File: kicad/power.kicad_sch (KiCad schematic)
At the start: 27 parts, among them U2 RT9471GQW, U3 MCP1663T-E/MNY, U4 MCP1603-330I/MC

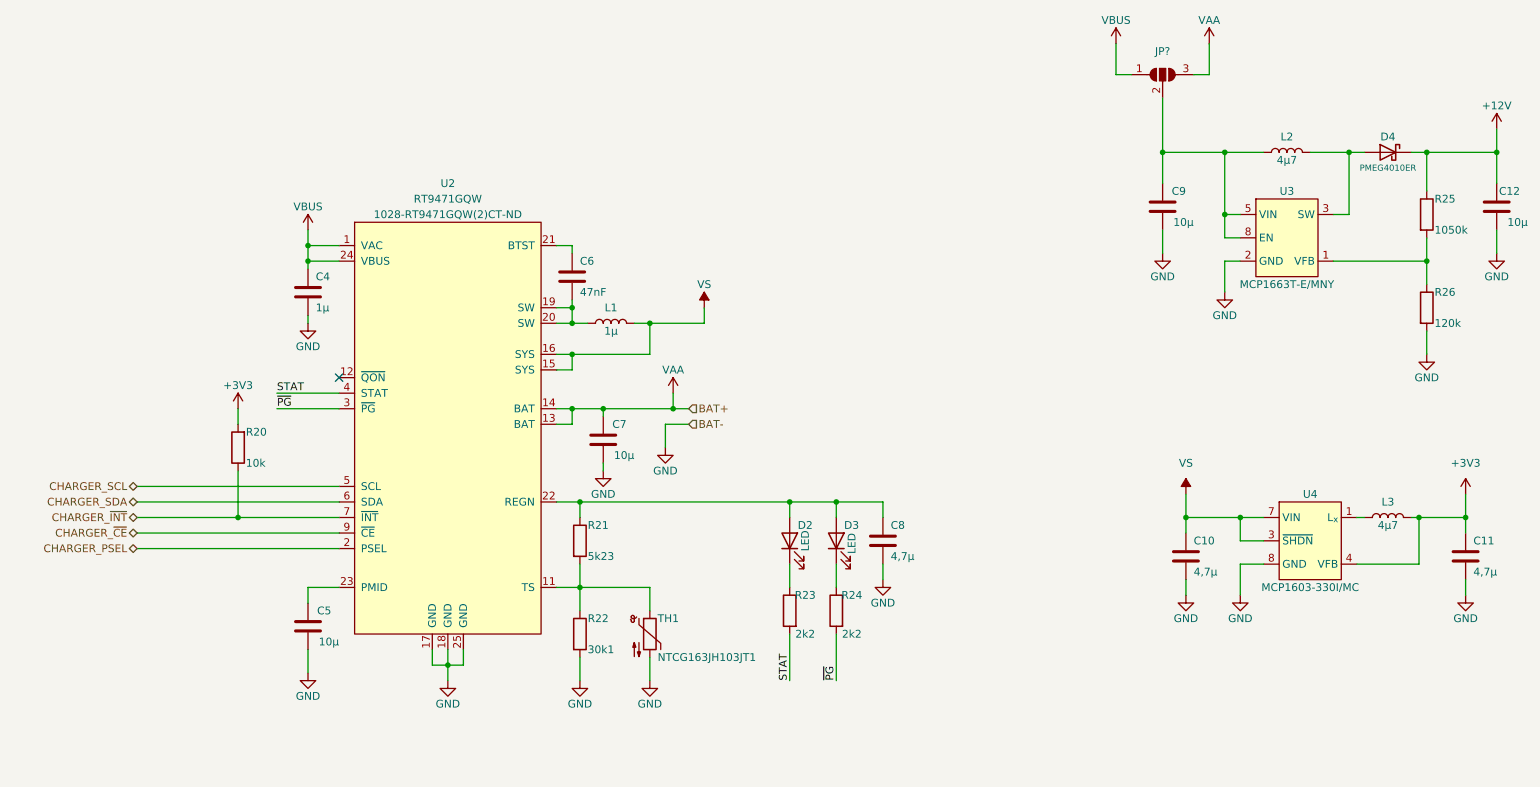
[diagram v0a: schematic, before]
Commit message: refactor KiCAD Project to v6
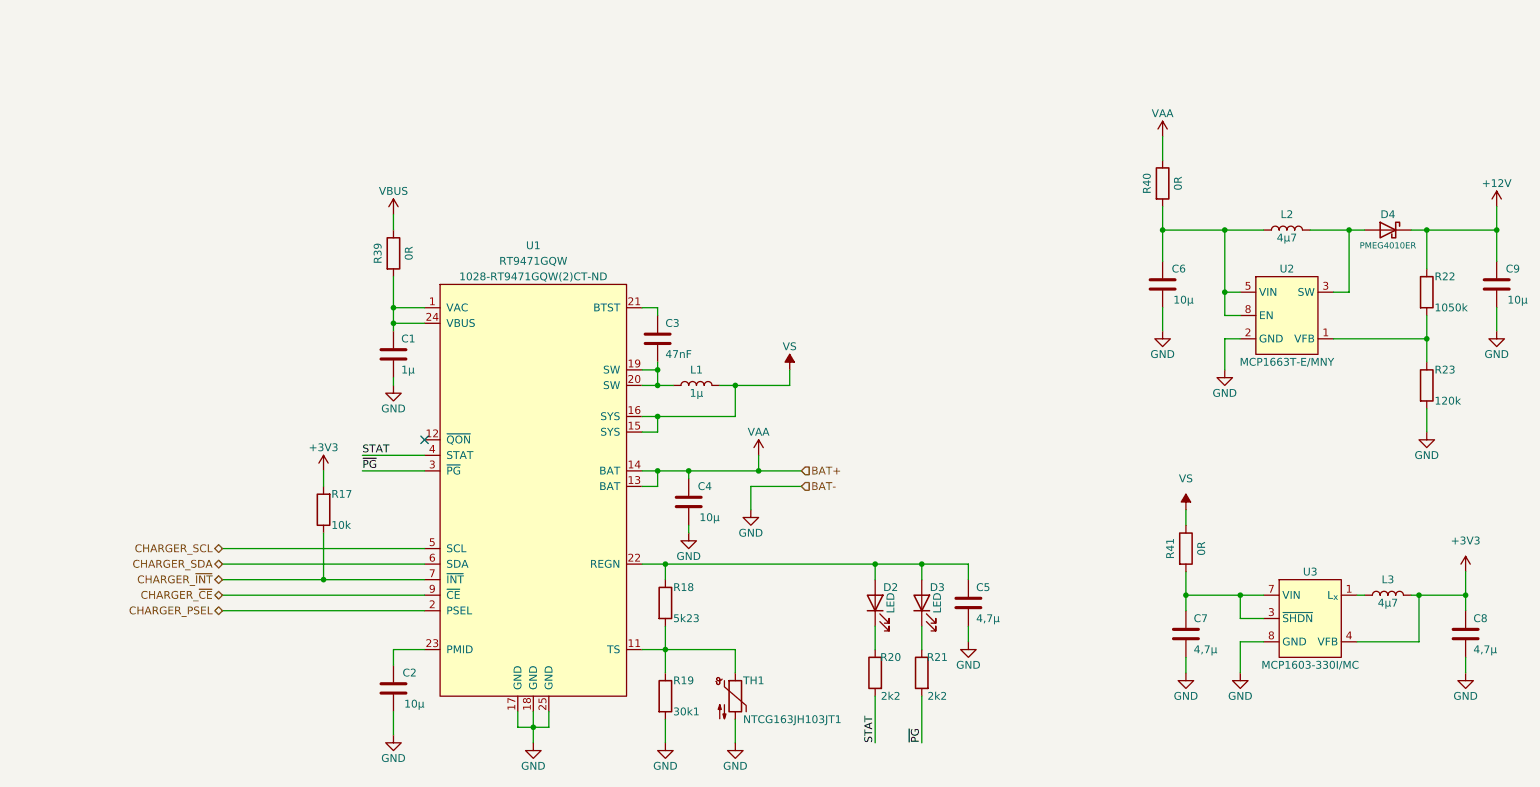
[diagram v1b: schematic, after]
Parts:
- removed C10, C11: 4,7µ, Capacitor_SMD:C_0603_1608Metric, symbol Device:C
- removed C12: 10µ, Capacitor_SMD:C_0603_1608Metric, symbol Device:C
- removed JP?: SolderJumper_3_Open, Jumper:SolderJumper-3_P1.3mm_Open_Pad1.0x1.5mm_NumberLabels, symbol Jumper:SolderJumper_3_Open
- removed R24: 2k2, Resistor_SMD:R_0603_1608Metric, symbol Device:R
- removed R25: 1050k, Resistor_SMD:R_0603_1608Metric, symbol Device:R
- removed R26: 120k, Resistor_SMD:R_0603_1608Metric, symbol Device:R
- removed U2: RT9471GQW, Package_DFN_QFN:WQFN-24-1EP_4x4mm_P0.5mm_EP2.6x2.6mm_ThermalVias, symbol z_ic:RT9471GQW
- removed U3: MCP1663T-E/MNY, Package_DFN_QFN:DFN-8-1EP_3x2mm_P0.5mm_EP1.36x1.46mm, symbol z_ic:MCP1663T-E/MNY
- removed U4: MCP1603-330I/MC, Package_DFN_QFN:DFN-8-1EP_3x2mm_P0.5mm_EP1.36x1.46mm, symbol z_ic:MCP1603-330I/MC
- added C1: 1µ, Capacitor_SMD:C_0603_1608Metric, symbol Device:C
- added C2: 10µ, Capacitor_SMD:C_0603_1608Metric, symbol Device:C
- added C3: 47nF, Capacitor_SMD:C_0603_1608Metric, symbol Device:C
- added R17: 10k, Resistor_SMD:R_0603_1608Metric, symbol Device:R
- added R18: 5k23, Resistor_SMD:R_0603_1608Metric, symbol Device:R
- added R19: 30k1, Resistor_SMD:R_0603_1608Metric, symbol Device:R
- added R39, R40, R41: 0R, Resistor_SMD:R_0603_1608Metric, symbol Device:R
- added U1: RT9471GQW, Package_DFN_QFN:WQFN-24-1EP_4x4mm_P0.5mm_EP2.6x2.6mm_ThermalVias, symbol z_ic:RT9471GQW
- added U2: MCP1663T-E/MNY, Package_DFN_QFN:DFN-8-1EP_3x2mm_P0.5mm_EP1.36x1.46mm, symbol z_ic:MCP1663T-E/MNY
- added U3: MCP1603-330I/MC, Package_DFN_QFN:DFN-8-1EP_3x2mm_P0.5mm_EP1.36x1.46mm, symbol z_ic:MCP1603-330I/MC
- C4: value 1µ -> 10µ; Digikey (none) -> 490-18214-1-ND
- C5, C7: value 10µ -> 4,7µ; Digikey (none) -> 1276-1045-1-ND
- C6: value 47nF -> 10µ; Digikey (none) -> 490-18214-1-ND
- C8: Digikey (none) -> 1276-1045-1-ND
- C9: Digikey (none) -> 490-18214-1-ND
- D2, D3: footprint (none) -> LED_SMD:LED_0603_1608Metric; Digikey (none) -> 516-HSMS-C197CT-ND
- D4: Digikey 1727-5213-1-ND -> 1727-7479-1-ND
- L1: footprint (none) -> Inductor_SMD:L_1008_2520Metric; Digikey (none) -> 1276-6929-1-ND
- R20: value 10k -> 2k2; Digikey (none) -> 311-2.20KHRCT-ND
- R21: value 5k23 -> 2k2; Digikey (none) -> 311-2.20KHRCT-ND
- R22: value 30k1 -> 1050k; Digikey (none) -> RMCF0603FT1M05CT-ND
- R23: value 2k2 -> 120k; Digikey (none) -> A129713CT-ND
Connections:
- net +12V: now also C9.1, R22.1
- net +3V3: now also C8.1, R17.2, U3.4 (VFB); no longer R20.2
- net CHARGER_PSEL: now also U1.2 (PSEL)
- net CHARGER_SCL: now also U1.5 (SCL)
- net CHARGER_SDA: now also U1.6 (SDA)
- net CHARGER_~{CE}: now also U1.9 (~{CE})
- net CHARGER_~{INT}: now also R17.1, U1.7 (~{INT}); no longer R20.1
- net GND: now also C6.2, R23.2, C1.2, C2.2, R19.2, U1.17 (GND), U1.18 (GND), U1.25 (GND), U2.2 (GND), U2.7 (GND), U2.9 (GND), U3.8 (GND), U3.9 (GND); no longer R22.2
- net STAT: now also R20.2, U1.4 (STAT); no longer R23.2
- net VAA: now also C4.1, R40.1, U1.13 (BAT), U1.14 (BAT); no longer C7.1
- net VBUS: now also R39.1; no longer C4.1
- net VS: now also R41.1, U1.15 (SYS), U1.16 (SYS)
- net ~{PG}: now also R21.2, U1.3 (~{PG})
- net at L2.1: now also C6.1, R40.2, U2.5 (VIN), U2.8 (EN); no longer C9.1
- net at D3.1 (K): now also R21.1
- net at D4.2 (A), L2.2: now also U2.3 (SW)
- net at L1.1: now also C3.2, U1.19 (SW), U1.20 (SW); no longer C6.2
- net at L3.1: now also U3.1 (L_{x})
- net at D2.2 (A), D3.2 (A): now also C5.1, R18.1, U1.22 (REGN); no longer C8.1, R21.1
- net at D2.1 (K): now also R20.1; no longer R23.1
- new net: C3.1, U1.21 (BTST)
- new net: C2.1, U1.23 (PMID)
- new net: C7.1, R41.2, U3.3 (~{SHDN}), U3.7 (VIN)
- new net: C1.1, R39.2, U1.1 (VAC), U1.24 (VBUS)
- new net: U3.2, U3.5, U3.6
- new net: R18.2, R19.1, TH1.1, U1.11 (TS)
- new net: R22.2, R23.1, U2.1 (VFB)
- new net: U2.4, U2.6

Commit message: add connection to lcd
import parts into pcbnew
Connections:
- net at U2.4: no longer U2.6
- now unconnected: U3.2, U3.5, U3.6

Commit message: route complete pcb
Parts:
- U1: footprint Package_DFN_QFN:WQFN-24-1EP_4x4mm_P0.5mm_EP2.6x2.6mm_ThermalVias -> z_ic:WQFN-24-1EP_4x4mm_P0.5mm_EP2.6x2.6mm_ThermalVias
- renumbered R17 to R18, R39 to R19, R18 to R20, R19 to R21, R20 to R22, R21 to R23, R40 to R24, R41 to R25, R22 to R26, R23 to R27

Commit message: rework pcb
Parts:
- U1: symbol z_ic:RT9471GQW -> mylib_ic:RT9471GQW
- U2: symbol z_ic:MCP1663T-E/MNY -> mylib_ic:MCP1663T-E/MNY
- U3: symbol z_ic:MCP1603-330I/MC -> mylib_ic:MCP1603-330I/MC
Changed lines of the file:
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@@
     (pin "1")
   )
-  (symbol (lib_id "z_ic:MCP1603-330I{slash}MC") (at 224.79 115.57 0) (unit 1)
+  (symbol (lib_id "mylib_ic:MCP1603-330I{slash}MC") (at 224.79 115.57 0) (unit 1)
     (in_bom yes) (on_board yes)
     (property "Reference" "U3" (id 0) (at 224.79 107.95 0))
@@
     (pin "2")
   )
-  (symbol (lib_id "z_ic:RT9471GQW") (at 97.79 92.71 0) (unit 1)
+  (symbol (lib_id "mylib_ic:RT9471GQW") (at 97.79 92.71 0) (unit 1)
     (in_bom yes) (on_board yes)
     (property "Reference" "U1" (id 0) (at 97.79 54.61 0))
@@
     (pin "2")
   )
-  (symbol (lib_id "z_ic:MCP1663T-E{slash}MNY") (at 220.98 66.04 0) (unit 1)
+  (symbol (lib_id "mylib_ic:MCP1663T-E{slash}MNY") (at 220.98 66.04 0) (unit 1)
     (in_bom yes) (on_board yes)
     (property "Reference" "U2" (id 0) (at 220.98 58.42 0))
